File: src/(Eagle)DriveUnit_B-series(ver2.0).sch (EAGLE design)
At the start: 70 parts, among them IC1 A3921, IC2 CZ3A07, SW1 TVAF06-A020B-R, SW2 TVAF06-A020B-R, SW3 THAF01-NC-R, SW4 SS-12D00G3

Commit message: [remove:電流センサを取り除いた
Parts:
- removed IC2: CZ3A07, CZ3A07:CZ3A07
- removed JP1: (no value), con-jst-xh:03-JST
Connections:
- removed net VOUT: JP1.2
- net GND_IN: no longer IC2.OCD2, IC2.REF2, IC2.VSS1, JP1.1
- net SA: no longer IC2.IP
- net SB: no longer IC2.IN
- net VCC_IN: no longer JP1.3
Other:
- note removed: "80Aの場合 1.29314286[V]"
- note removed: "VREF1 [mV] = 2500 - |IOCDTH1|[A] × (528/35)"
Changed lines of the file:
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@@
 <part name="SUPPLY21" library="supply2" library_urn="urn:adsk.eagle:library:372" deviceset="GND" device=""/>
 <part name="R28" library="GF063P B104K" deviceset="GF063PB104K" device="" value="100k"/>
-<part name="FRAME2" library="frames" library_urn="urn:adsk.eagle:library:229" deviceset="A5L-LOC" device=""/>
-<part name="IC2" library="CZ3A07" deviceset="CZ3A07" device=""/>
-<part name="JP1" library="con-jst-xh" deviceset="03-JST" device=""/>
 </parts>
 <sheets>
@@
 <wire x1="115.824" y1="203.2" x2="129.54" y2="203.2" width="0.1524" layer="91"/>
 <junction x="129.54" y="203.2"/>
-<wire x1="129.54" y1="203.2" x2="180.34" y2="203.2" width="0.1524" layer="91"/>
 <label x="177.8" y="203.2" size="1.778" layer="95"/>
 </segment>
@@
 </segment>
 </net>
-</nets>
-</sheet>
-<sheet>
-<plain>
-<text x="140.97" y="20.32" size="2.54" layer="94">2020年度回路班</text>
-<text x="48.26" y="79.502" size="1.778" layer="91">+put</text>
-<text x="48.26" y="69.342" size="1.778" layer="91">-put</text>
-<text x="50.8" y="96.52" size="1.27" layer="97">VREF1 [mV] = 2500 - |IOCDTH1|[A] × (528/35)</text>
-<text x="63.5" y="91.44" size="1.27" layer="97">80Aの場合
-1.29314286[V]</text>
-</plain>
-<instances>
-<instance part="FRAME2" gate="G$1" x="0" y="0" smashed="yes">
-<attribute name="DRAWING_NAME" x="140.97" y="15.24" size="2.54" layer="94"/>
-<attribute name="LAST_DATE_TIME" x="140.97" y="10.16" size="2.286" layer="94"/>
-<attribute name="SHEET" x="154.305" y="5.08" size="2.54" layer="94"/>
-</instance>
-<instance part="IC2" gate="G$1" x="66.294" y="74.93" smashed="yes">
-<attribute name="NAME" x="59.944" y="85.725" size="1.778" layer="95"/>
-<attribute name="VALUE" x="59.944" y="59.69" size="1.778" layer="96"/>
-</instance>
-<instance part="JP1" gate="G$1" x="134.62" y="73.66" smashed="yes">
-<attribute name="VALUE" x="133.35" y="66.04" size="1.778" layer="96"/>
-<attribute name="NAME" x="133.35" y="79.502" size="1.778" layer="95"/>
-</instance>
-</instances>
-<busses>
-</busses>
-<nets>
-<net name="SA" class="0">
-<segment>
-<pinref part="IC2" gate="G$1" pin="IP"/>
-<wire x1="63.754" y1="78.74" x2="48.26" y2="78.74" width="0.1524" layer="91"/>
-</segment>
-</net>
-<net name="SB" class="0">
-<segment>
-<pinref part="IC2" gate="G$1" pin="IN"/>
-<wire x1="63.754" y1="68.58" x2="48.26" y2="68.58" width="0.1524" layer="91"/>
-</segment>
-</net>
-<net name="GND_IN" class="0">
-<segment>
-<pinref part="JP1" gate="G$1" pin="1"/>
-<wire x1="142.24" y1="71.12" x2="147.32" y2="71.12" width="0.1524" layer="91"/>
-<wire x1="147.32" y1="71.12" x2="147.32" y2="66.04" width="0.1524" layer="91"/>
-<label x="142.24" y="63.5" size="2.54" layer="95"/>
-</segment>
-<segment>
-<pinref part="IC2" gate="G$1" pin="VSS1"/>
-<wire x1="71.374" y1="64.77" x2="93.98" y2="64.77" width="0.1524" layer="91"/>
-<wire x1="93.98" y1="64.77" x2="93.98" y2="53.34" width="0.1524" layer="91"/>
-<label x="93.98" y="53.34" size="2.54" layer="95"/>
-<pinref part="IC2" gate="G$1" pin="REF2"/>
-<wire x1="71.374" y1="80.01" x2="93.98" y2="80.01" width="0.1524" layer="91"/>
-<wire x1="93.98" y1="80.01" x2="93.98" y2="69.85" width="0.1524" layer="91"/>
-<junction x="93.98" y="64.77"/>
-<pinref part="IC2" gate="G$1" pin="OCD2"/>
-<wire x1="93.98" y1="69.85" x2="93.98" y2="64.77" width="0.1524" layer="91"/>
-<wire x1="71.374" y1="69.85" x2="93.98" y2="69.85" width="0.1524" layer="91"/>
-<junction x="93.98" y="69.85"/>
-</segment>
-</net>
-<net name="VCC_IN" class="0">
-<segment>
-<pinref part="JP1" gate="G$1" pin="3"/>
-<wire x1="142.24" y1="76.2" x2="147.32" y2="76.2" width="0.1524" layer="91"/>
-<wire x1="147.32" y1="76.2" x2="147.32" y2="83.82" width="0.1524" layer="91"/>
-<label x="142.24" y="83.82" size="2.54" layer="95"/>
-</segment>
-</net>
-<net name="VOUT" class="0">
-<segment>
-<pinref part="JP1" gate="G$1" pin="2"/>
-<wire x1="142.24" y1="73.66" x2="157.48" y2="73.66" width="0.1524" layer="91"/>
-<label x="149.86" y="73.66" size="2.54" layer="95"/>
-</segment>
-</net>

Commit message: [add]配線の追加
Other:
- note removed: "ブートストラップ→一般式912/13.75[nF] 0.066[uF]近くにする→0.1[uF]に訂正"
- note removed: "充電時間 MD動作中→0.46[us] 訂正後 0.6[us] 電源投入時→9.1[us] 訂正後 12[us]"
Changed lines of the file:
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@@
 だけソースと繋げる</text>
 <text x="141.732" y="92.202" size="1.778" layer="95">逆電圧防止</text>
-<text x="152.654" y="110.49" size="1.778" layer="95">ブートストラップ→一般式912/13.75[nF]
-0.066[uF]近くにする→0.1[uF]に訂正</text>
 <text x="68.58" y="99.06" size="1.778" layer="95">パスコンくん</text>
 <text x="58.42" y="116.84" size="1.016" layer="95">プルアップ抵抗(RESETをGNDに接続するとRESET)</text>
@@
 <text x="140.208" y="64.77" size="1.778" layer="95">V5</text>
 <text x="73.66" y="220.98" size="1.778" layer="95">正転</text>
-<text x="177.546" y="115.57" size="1.016" layer="95">充電時間
-MD動作中→0.46[us] 訂正後 0.6[us]
-電源投入時→9.1[us] 訂正後 12[us]</text>
 <text x="93.98" y="132.08" size="1.778" layer="95">0.180[us]</text>
 <text x="269.24" y="170.942" size="1.778" layer="91">+put</text>
@@
 <pinref part="R9" gate="G$1" pin="LEFT"/>
 <wire x1="129.54" y1="217.678" x2="129.54" y2="213.36" width="0.1524" layer="91"/>
-<wire x1="129.54" y1="213.36" x2="129.54" y2="203.2" width="0.1524" layer="91"/>
+<wire x1="129.54" y1="213.36" x2="129.54" y2="205.74" width="0.1524" layer="91"/>
 <junction x="129.54" y="213.36"/>
 <wire x1="155.956" y1="213.36" x2="129.54" y2="213.36" width="0.1524" layer="91"/>
@@
 <junction x="129.54" y="203.2"/>
 <label x="177.8" y="203.2" size="1.778" layer="95"/>
-</segment>
-<segment>
+<wire x1="129.54" y1="205.74" x2="129.54" y2="203.2" width="0.1524" layer="91"/>
+<wire x1="129.54" y1="203.2" x2="182.88" y2="203.2" width="0.1524" layer="91"/>
+</segment>
+<segment>

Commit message: [add]配線の追加
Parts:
- renumbered 3813-HA to HA, 3813-HB to HB, 3813-LA to LA, 3813-LB to LB
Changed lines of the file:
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@@
 <parts>
 <part name="FRAME1" library="frames" library_urn="urn:adsk.eagle:library:229" deviceset="A3L-LOC" device=""/>
-<part name="3813-HA" library="OKUDA_libraries" deviceset="IRLB3813" device="NOHOLE"/>
-<part name="3813-LA" library="OKUDA_libraries" deviceset="IRLB3813" device="NOHOLE"/>
-<part name="3813-HB" library="OKUDA_libraries" deviceset="IRLB3813" device="NOHOLE"/>
-<part name="3813-LB" library="OKUDA_libraries" deviceset="IRLB3813" device="NOHOLE"/>
+<part name="HA" library="OKUDA_libraries" deviceset="IRLB3813" device="NOHOLE"/>
+<part name="LA" library="OKUDA_libraries" deviceset="IRLB3813" device="NOHOLE"/>
+<part name="HB" library="OKUDA_libraries" deviceset="IRLB3813" device="NOHOLE"/>
+<part name="LB" library="OKUDA_libraries" deviceset="IRLB3813" device="NOHOLE"/>
 <part name="P+1" library="supply1" library_urn="urn:adsk.eagle:library:371" deviceset="VCC" device="" value="+BATT"/>
 <part name="SUPPLY1" library="supply2" library_urn="urn:adsk.eagle:library:372" deviceset="GND" device=""/>
@@
 <attribute name="SHEET" x="357.505" y="5.08" size="2.54" layer="94"/>
 </instance>
-<instance part="3813-HA" gate="G$1" x="266.7" y="187.96" smashed="yes">
+<instance part="HA" gate="G$1" x="266.7" y="187.96" smashed="yes">
 <attribute name="NAME" x="268.605" y="186.055" size="0.8128" layer="95" rot="R90"/>
 </instance>
-<instance part="3813-LA" gate="G$1" x="266.7" y="152.4" smashed="yes">
+<instance part="LA" gate="G$1" x="266.7" y="152.4" smashed="yes">
 <attribute name="NAME" x="268.605" y="150.495" size="0.8128" layer="95" rot="R90"/>
 </instance>
-<instance part="3813-HB" gate="G$1" x="314.96" y="187.96" smashed="yes" rot="MR0">
+<instance part="HB" gate="G$1" x="314.96" y="187.96" smashed="yes" rot="MR0">
 <attribute name="NAME" x="313.055" y="186.055" size="0.8128" layer="95" rot="MR90"/>
 </instance>
-<instance part="3813-LB" gate="G$1" x="314.96" y="152.4" smashed="yes" rot="MR0">
+<instance part="LB" gate="G$1" x="314.96" y="152.4" smashed="yes" rot="MR0">
 <attribute name="NAME" x="313.055" y="150.495" size="0.8128" layer="95" rot="MR90"/>
 </instance>
@@
 </segment>
 <segment>
-<pinref part="3813-HA" gate="G$1" pin="D"/>
+<pinref part="HA" gate="G$1" pin="D"/>
 <wire x1="266.7" y1="190.5" x2="266.7" y2="205.74" width="0.1524" layer="91"/>
 <wire x1="266.7" y1="205.74" x2="289.56" y2="205.74" width="0.1524" layer="91"/>
-<pinref part="3813-HB" gate="G$1" pin="D"/>
+<pinref part="HB" gate="G$1" pin="D"/>
 <wire x1="289.56" y1="205.74" x2="314.96" y2="205.74" width="0.1524" layer="91"/>
 <wire x1="314.96" y1="205.74" x2="314.96" y2="190.5" width="0.1524" layer="91"/>
@@
 </segment>
 <segment>
-<pinref part="3813-LA" gate="G$1" pin="S"/>
-<pinref part="3813-LB" gate="G$1" pin="S"/>
+<pinref part="LA" gate="G$1" pin="S"/>
+<pinref part="LB" gate="G$1" pin="S"/>
 <wire x1="266.7" y1="149.86" x2="266.7" y2="134.62" width="0.1524" layer="91"/>
 <wire x1="266.7" y1="134.62" x2="289.56" y2="134.62" width="0.1524" layer="91"/>
@@
 </segment>
 <segment>
-<pinref part="3813-HB" gate="G$1" pin="S"/>
-<pinref part="3813-LB" gate="G$1" pin="D"/>
+<pinref part="HB" gate="G$1" pin="S"/>
+<pinref part="LB" gate="G$1" pin="D"/>
 <wire x1="314.96" y1="185.42" x2="314.96" y2="170.18" width="0.1524" layer="91"/>
 <wire x1="314.96" y1="170.18" x2="314.96" y2="154.94" width="0.1524" layer="91"/>
@@
 </segment>
 <segment>
-<pinref part="3813-HA" gate="G$1" pin="S"/>
-<pinref part="3813-LA" gate="G$1" pin="D"/>
+<pinref part="HA" gate="G$1" pin="S"/>
+<pinref part="LA" gate="G$1" pin="D"/>
 <wire x1="266.7" y1="185.42" x2="266.7" y2="170.18" width="0.1524" layer="91"/>
 <wire x1="266.7" y1="170.18" x2="266.7" y2="154.94" width="0.1524" layer="91"/>
@@
 <net name="N$25" class="0">
 <segment>
-<pinref part="3813-LA" gate="G$1" pin="G"/>
+<pinref part="LA" gate="G$1" pin="G"/>
 <wire x1="261.62" y1="149.86" x2="261.62" y2="154.94" width="0.1524" layer="91"/>
 <wire x1="261.62" y1="154.94" x2="259.08" y2="154.94" width="0.1524" layer="91"/>
@@
 <segment>
 <wire x1="325.12" y1="149.86" x2="325.12" y2="154.94" width="0.1524" layer="91"/>
-<pinref part="3813-LB" gate="G$1" pin="G"/>
+<pinref part="LB" gate="G$1" pin="G"/>
 <wire x1="320.04" y1="149.86" x2="320.04" y2="154.94" width="0.1524" layer="91"/>
 <wire x1="320.04" y1="154.94" x2="325.12" y2="154.94" width="0.1524" layer="91"/>
@@
 <net name="N$13" class="0">
 <segment>
-<pinref part="3813-HA" gate="G$1" pin="G"/>
+<pinref part="HA" gate="G$1" pin="G"/>
 <wire x1="261.62" y1="190.5" x2="261.62" y2="185.42" width="0.1524" layer="91"/>
 <wire x1="261.62" y1="190.5" x2="259.08" y2="190.5" width="0.1524" layer="91"/>
@@
 <net name="N$21" class="0">
 <segment>
-<pinref part="3813-HB" gate="G$1" pin="G"/>
+<pinref part="HB" gate="G$1" pin="G"/>
 <wire x1="320.04" y1="185.42" x2="320.04" y2="190.5" width="0.1524" layer="91"/>
 <wire x1="320.04" y1="190.5" x2="325.12" y2="190.5" width="0.1524" layer="91"/>

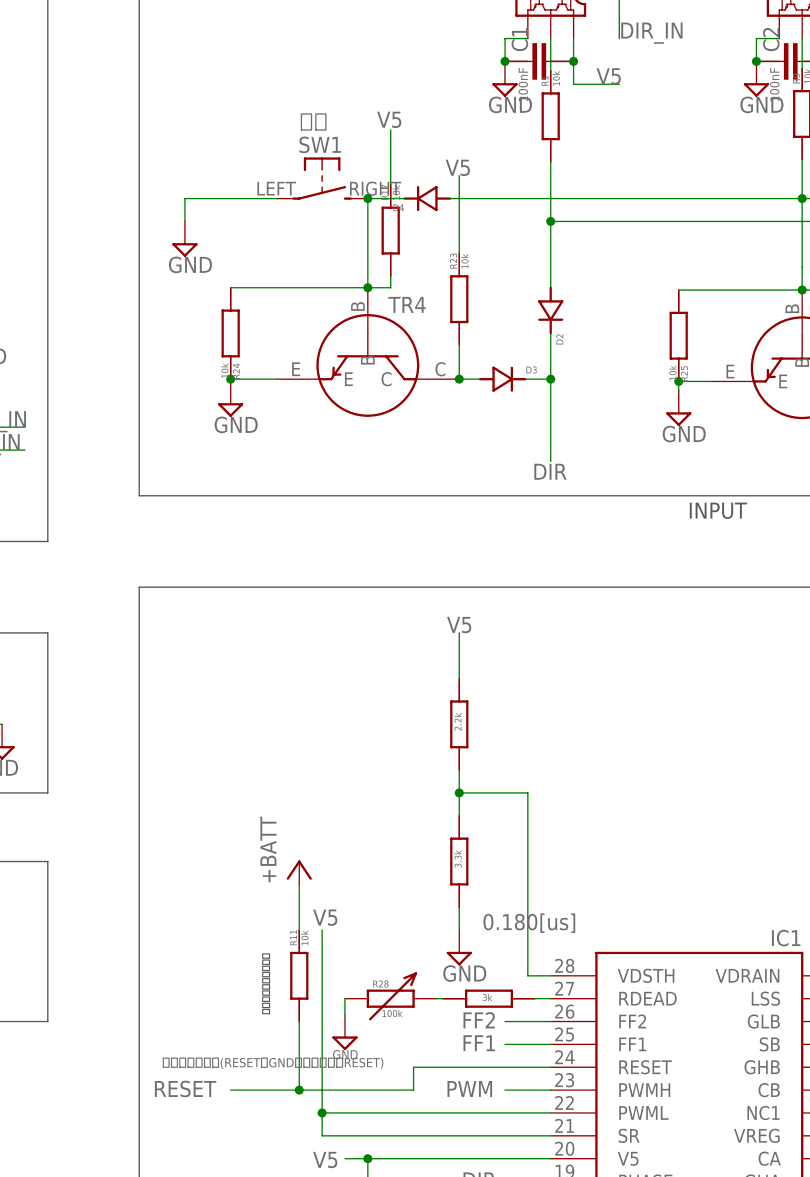
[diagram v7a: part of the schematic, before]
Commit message: 入力部の配線の追加
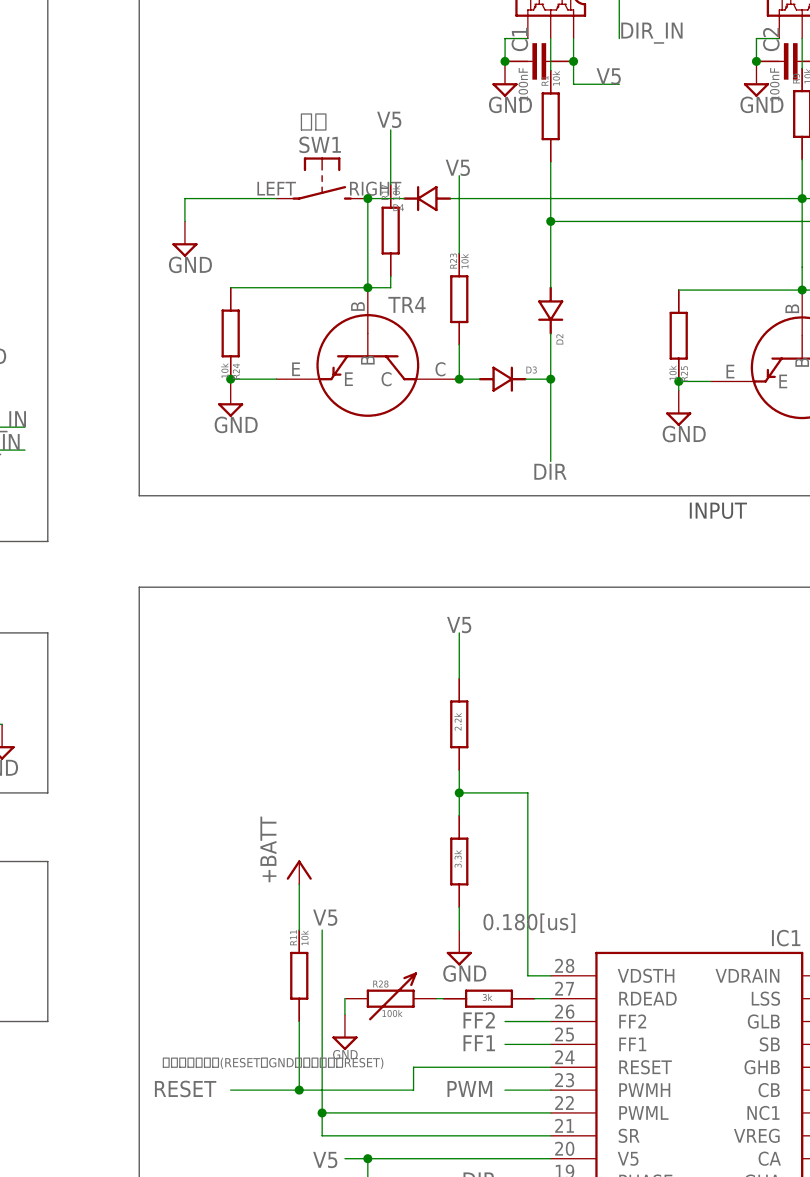
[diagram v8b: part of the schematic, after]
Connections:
- new net N$27: D2.A, D6.A, R1.LEFT
- net DIR: no longer D2.A, D6.A, R1.LEFT
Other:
- note removed: "プルアップ抵抗は適当"
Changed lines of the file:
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@@
 <text x="22.86" y="144.78" size="1.778" layer="97">SM/LAP</text>
 <text x="22.86" y="119.38" size="1.778" layer="97">Reset</text>
-<text x="70.358" y="122.682" size="0.762" layer="97" rot="R90">プルアップ抵抗は適当</text>
 <wire x1="63.5" y1="7.62" x2="190.5" y2="7.62" width="0.1524" layer="97"/>
 <text x="170.18" y="220.98" size="1.778" layer="95">逆転</text>
@@
 </segment>
 <segment>
-<pinref part="R1" gate="G$1" pin="LEFT"/>
-<wire x1="101.6" y1="217.424" x2="101.6" y2="210.82" width="0.1524" layer="91"/>
-<wire x1="155.956" y1="210.82" x2="101.6" y2="210.82" width="0.1524" layer="91"/>
-<pinref part="D6" gate="G$1" pin="A"/>
-<pinref part="D2" gate="G$1" pin="A"/>
-<wire x1="101.6" y1="210.82" x2="101.6" y2="203.454" width="0.1524" layer="91"/>
-<junction x="101.6" y="210.82"/>
-</segment>
-<segment>
 <pinref part="D3" gate="G$1" pin="C"/>
 <wire x1="98.806" y1="193.294" x2="101.6" y2="193.294" width="0.1524" layer="91"/>
@@
 </segment>
 </net>
+<net name="N$27" class="0">
+<segment>
+<pinref part="D2" gate="G$1" pin="A"/>
+<pinref part="R1" gate="G$1" pin="LEFT"/>
+<wire x1="101.6" y1="203.454" x2="101.6" y2="210.82" width="0.1524" layer="91"/>
+<pinref part="D6" gate="G$1" pin="A"/>
+<wire x1="101.6" y1="210.82" x2="101.6" y2="217.424" width="0.1524" layer="91"/>
+<wire x1="155.956" y1="210.82" x2="101.6" y2="210.82" width="0.1524" layer="91"/>
+<junction x="101.6" y="210.82"/>
+</segment>
+</net>
